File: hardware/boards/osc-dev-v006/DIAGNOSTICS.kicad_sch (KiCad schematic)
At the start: 28 parts

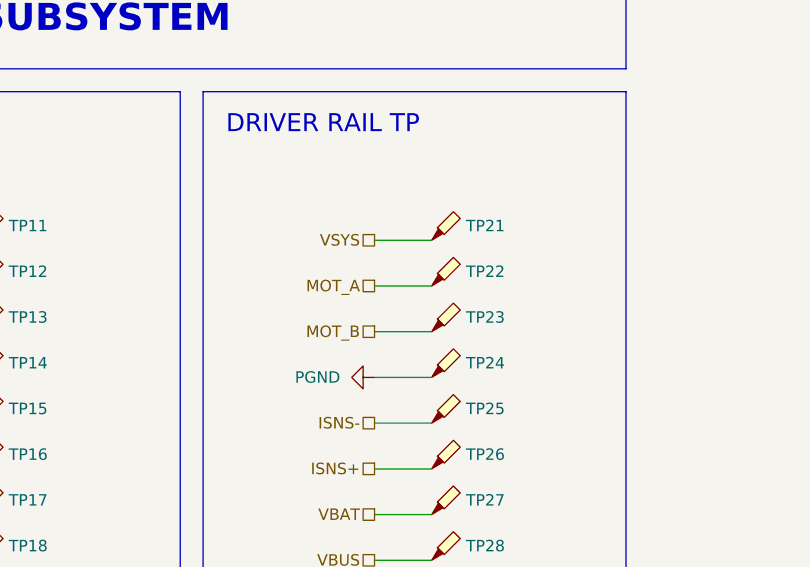
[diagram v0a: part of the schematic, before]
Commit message: OSC DEV CH32 REV B (#10)
* update board

* updated schematics. ERC on schematics is now passing

* completed routing.

* adding ground vias

* update schematics notes

* update bom and component properties

* use red header pins for jumpers

* rename board to osc-dev-v006

* add docs
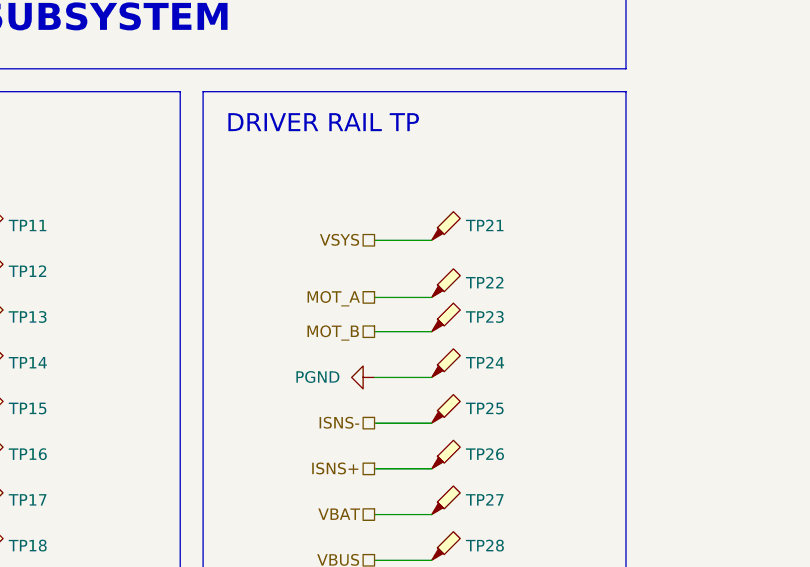
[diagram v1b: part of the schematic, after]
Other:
- moved on the sheet: TP22
